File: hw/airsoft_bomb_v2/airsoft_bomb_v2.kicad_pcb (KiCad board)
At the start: 2 copper layers, 71.4 x 76.7 mm, 52 parts, among them J1 Conn_01x10_Pin, J2 Conn_01x16_Pin, J3 BTN_R, J4 BTN_Y, J5 SIREN, J6 Conn_01x02_Socket, Q2 AO3400A, Q4 AO3400A, Q5 AO3400A, U1 PCF8574, U2 PCF8574, U4 LM317_SOT-223

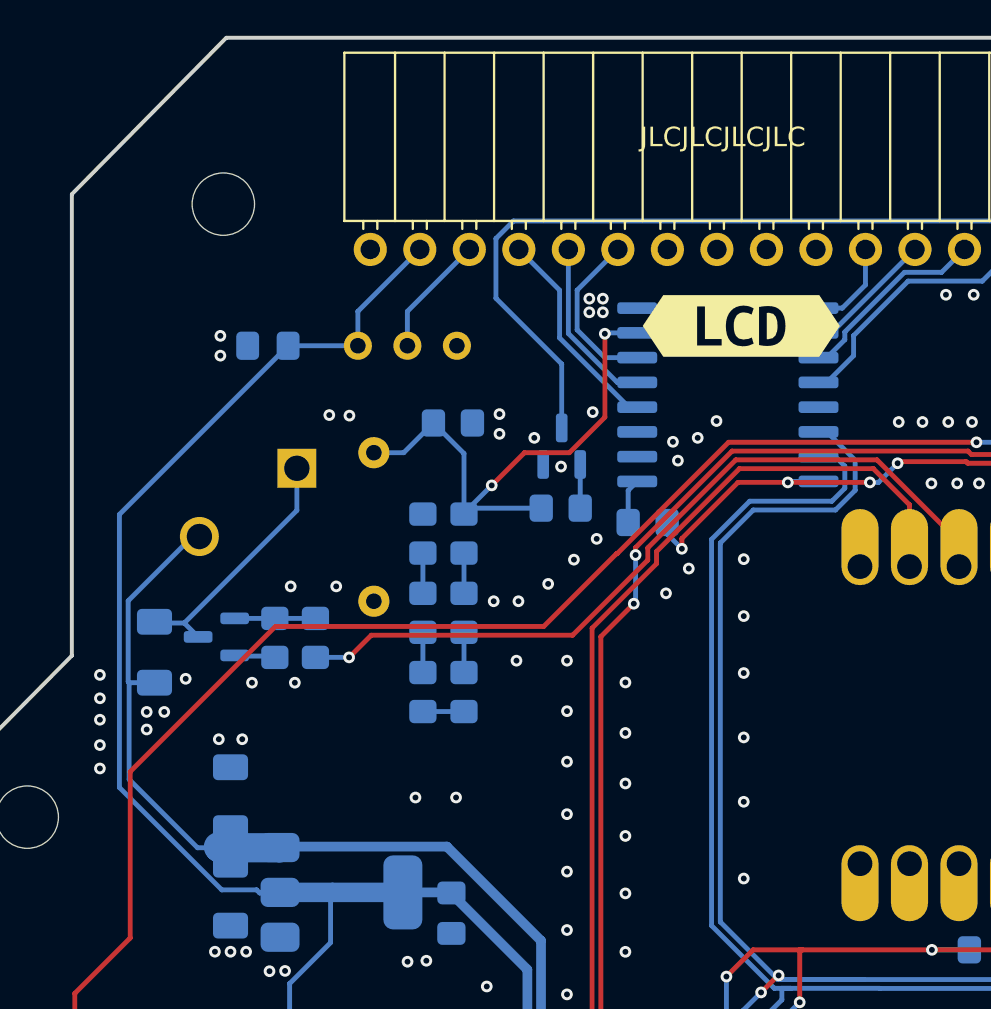
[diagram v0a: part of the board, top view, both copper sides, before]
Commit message: add kibot.sh and required fixes
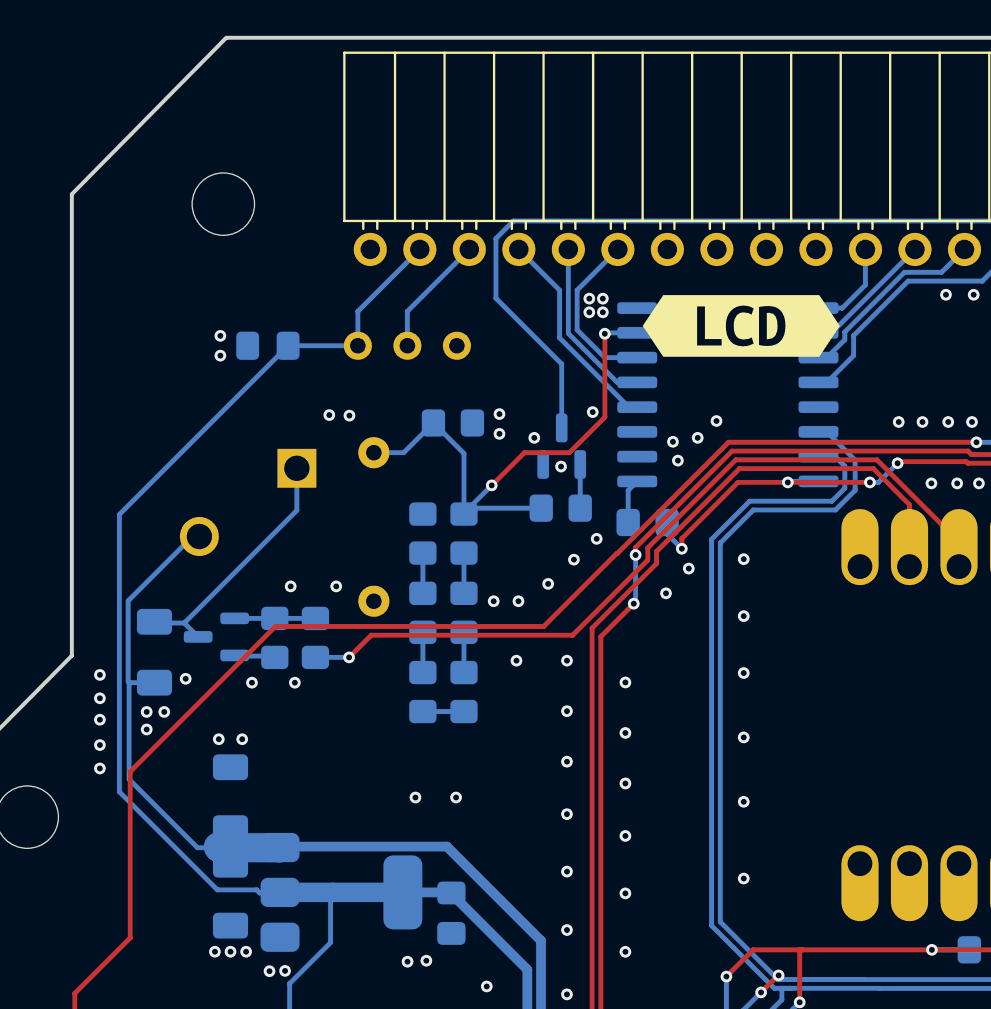
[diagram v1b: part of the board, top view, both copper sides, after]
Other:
- board text removed: "JLCJLCJLCJLC"
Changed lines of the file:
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@@
 		(sheetname "Root")
 		(sheetfile "airsoft_bomb_v2.kicad_sch")
-		(attr smd)
+		(attr smd exclude_from_bom dnp)
 		(fp_line
 			(start 0.227064 0.735)
@@
 		(sheetname "Root")
 		(sheetfile "airsoft_bomb_v2.kicad_sch")
-		(attr smd)
+		(attr smd exclude_from_bom dnp)
 		(fp_line
 			(start 0.227064 0.735)
@@
 		(sheetname "Root")
 		(sheetfile "airsoft_bomb_v2.kicad_sch")
-		(attr smd)
+		(attr smd exclude_from_bom dnp)
 		(fp_line
 			(start 0.227064 0.735)
@@
 		(sheetname "Root")
 		(sheetfile "airsoft_bomb_v2.kicad_sch")
-		(attr through_hole exclude_from_bom dnp)
+		(attr through_hole)
 		(fp_line
 			(start 7.08 -1.37)
@@
 		(sheetname "Root")
 		(sheetfile "airsoft_bomb_v2.kicad_sch")
-		(attr smd)
+		(attr smd exclude_from_bom dnp)
 		(fp_line
 			(start 0.227064 -0.735)
@@
 		(sheetname "Root")
 		(sheetfile "airsoft_bomb_v2.kicad_sch")
-		(attr smd)
+		(attr smd exclude_from_bom dnp)
 		(fp_line
 			(start 0.227064 -0.735)
@@
 		(sheetname "Root")
 		(sheetfile "airsoft_bomb_v2.kicad_sch")
-		(attr smd dnp)
+		(attr smd exclude_from_bom dnp)
 		(fp_line
 			(start 0.227064 0.735)
@@
 		(sheetname "Root")
 		(sheetfile "airsoft_bomb_v2.kicad_sch")
-		(attr smd)
+		(attr smd exclude_from_bom dnp)
 		(fp_line
 			(start 0.227064 -0.735)
@@
 		)
 	)
-	(gr_text "JLCJLCJLCJLC"
-		(at 147.2 63.9 0)
-		(layer "F.SilkS")
-		(effects
-			(font
-				(size 1 1)
-				(thickness 0.1)
-			)
-			(justify left bottom)
-		)
-	)
 	(segment
 		(start 153.0096 105.0036)
@@
 	)
 	(segment
-		(start 120.5 96.6748)
+		(start 120.5 96.9)
 		(end 120.5 82.6707)
 		(width 0.25)
@@
 	)
 	(segment
-		(start 120.5 82.6707)
-		(end 129.1551 74.0156)
-		(width 0.25)
-		(layer "B.Cu")
-		(net 4)
-	)
-	(segment
 		(start 131.3319 104.6341)
 		(end 131.3319 102.1588)
@@
 	)
 	(segment
-		(start 127.69513 102.0841)
-		(end 127.53923 101.9282)
-		(width 0.25)
-		(layer "B.Cu")
-		(net 4)
-	)
-	(segment
 		(start 176.27 85.344)
 		(end 176.27 76.415)
@@
 	)
 	(segment
-		(start 127.53923 101.9282)
-		(end 125.7534 101.9282)
-		(width 0.25)
-		(layer "B.Cu")
-		(net 4)
-	)
-	(segment
 		(start 137.4648 102.0572)
 		(end 141.4272 106.0196)
@@
 	)
 	(segment
+		(start 127.7407 102.0572)
+		(end 127.7138 102.0841)
+		(width 0.25)
+		(layer "B.Cu")
+		(net 4)
+	)
+	(segment
+		(start 127.69513 102.0841)
+		(end 127.53923 101.9282)
+		(width 0.25)
+		(layer "B.Cu")
+		(net 4)
+	)
+	(segment
 		(start 129.2315 124.9258)
 		(end 129.2315 106.7345)
@@
 	)
 	(segment
+		(start 127.53923 101.9282)
+		(end 125.5282 101.9282)
+		(width 0.25)
+		(layer "B.Cu")
+		(net 4)
+	)
+	(segment
 		(start 128.7407 102.0572)
-		(end 131.4335 102.0572)
-		(width 1)
+		(end 127.7407 102.0572)
+		(width 0.25)
 		(layer "B.Cu")
 		(net 4)
 	)
 	(segment
-		(start 125.7534 101.9282)
-		(end 120.5 96.6748)
+		(start 120.5 82.6707)
+		(end 129.1551 74.0156)
 		(width 0.25)
 		(layer "B.Cu")
@@
 	)
 	(segment
+		(start 128.7407 102.0572)
+		(end 131.4335 102.0572)
+		(width 1)
+		(layer "B.Cu")
+		(net 4)
+	)
+	(segment
 		(start 148.088139 115.6208)
 		(end 141.4272 108.959861)
@@
 	)
 	(segment
-		(start 127.7407 102.0572)
-		(end 127.7138 102.0841)
-		(width 0.25)
-		(layer "B.Cu")
-		(net 4)
-	)
-	(segment
-		(start 128.7407 102.0572)
-		(end 127.7407 102.0572)
+		(start 125.5282 101.9282)
+		(end 120.5 96.9)
 		(width 0.25)
 		(layer "B.Cu")
